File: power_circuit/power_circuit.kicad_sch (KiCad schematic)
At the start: 38 parts, among them J1 +, J10 Conn_01x02_Pin, J2 -, J7 Conn_01x02_Pin, M1 Fan, Q1 PMOS, Q2 PMOS, Q3 PMOS, Q4 PMOS, Q5 PMOS, Q6 PMOS, Q7 PMOS, Q8 PMOS, SW1 SW_SPDT, U1 LM76002RNPR, U2 STM32F042C6Tx, U3 TJA1051TK-3, U4 AMS1117-3.3

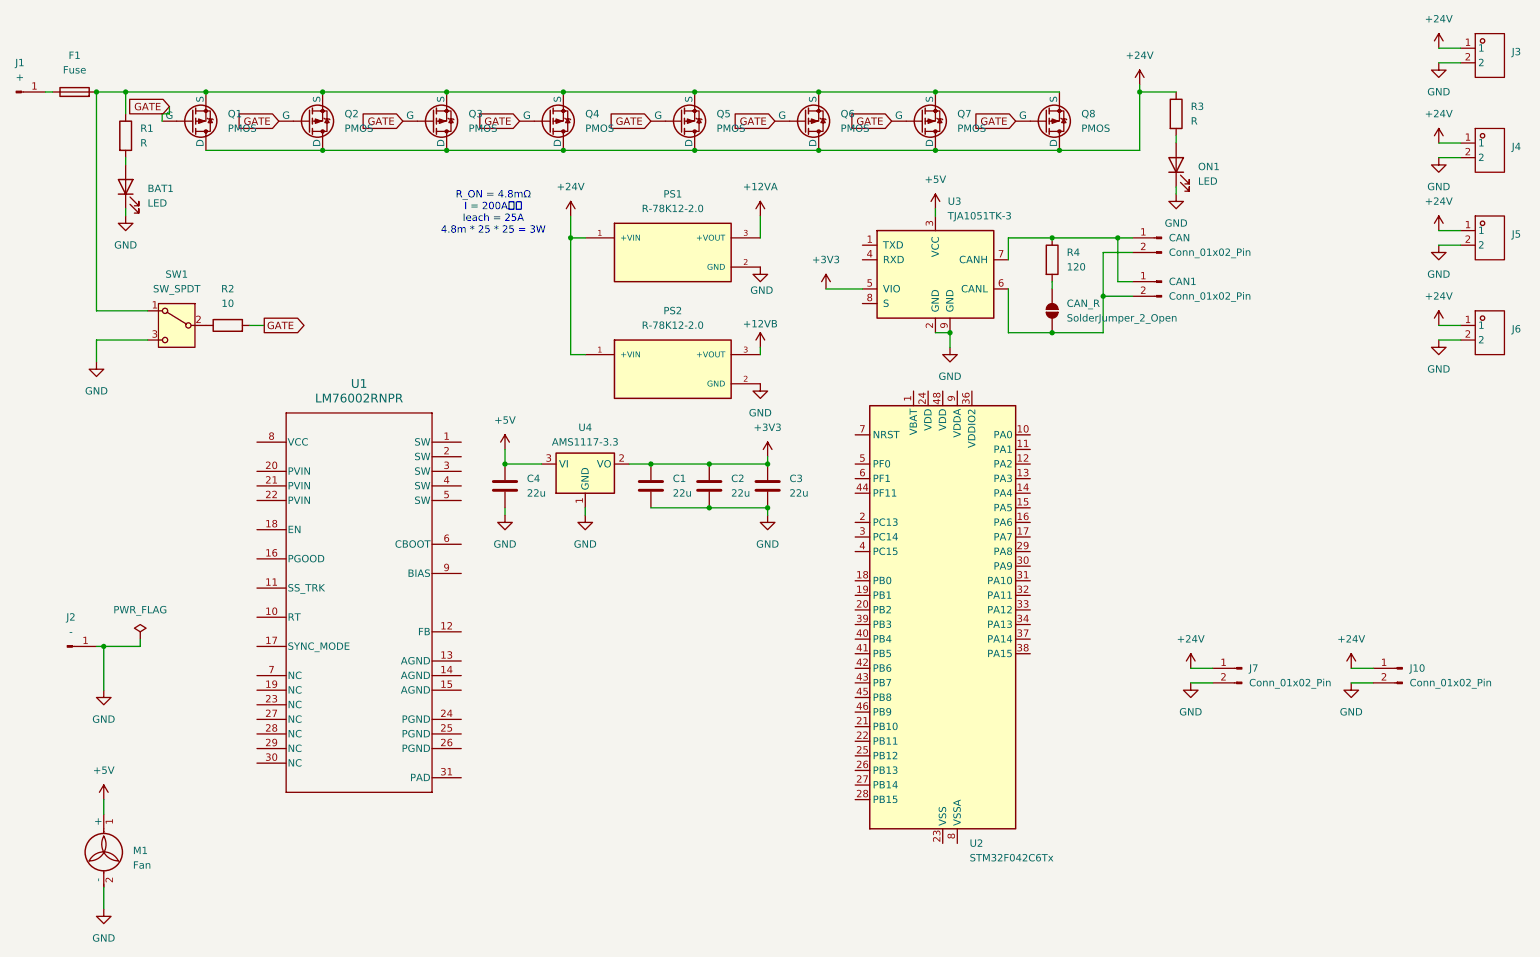
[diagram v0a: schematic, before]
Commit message: AQUA_VESC REV01作成
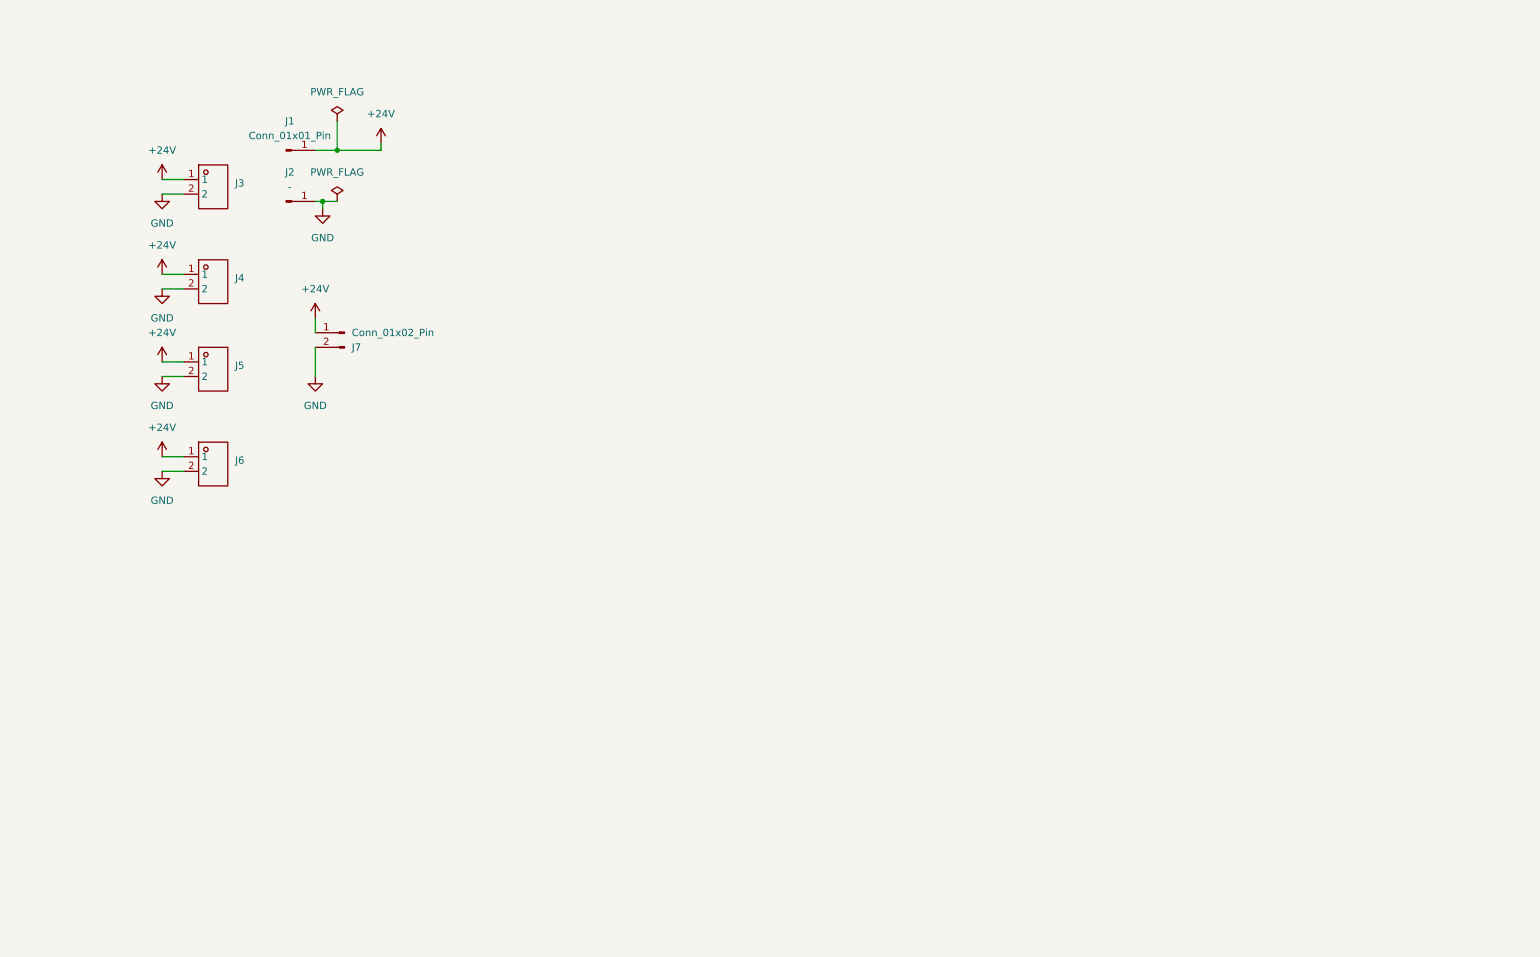
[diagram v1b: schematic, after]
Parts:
- removed BAT1, ON1: LED, symbol Device:LED
- removed C1, C2, C3, C4: 22u, symbol Device:C
- removed CAN, CAN1: Conn_01x02_Pin, Connector_JST:JST_XA_S02B-XASK-1_1x02_P2.50mm_Horizontal, symbol Connector:Conn_01x02_Pin
- removed CAN_R: SolderJumper_2_Open, symbol Jumper:SolderJumper_2_Open
- removed F1: Fuse, specific_footprint_library:anl_fuse, symbol Device:Fuse
- removed J10: Conn_01x02_Pin, Connector_JST:JST_VH_B2PS-VH_1x02_P3.96mm_Horizontal, symbol Connector:Conn_01x02_Pin
- removed M1: Fan, symbol Motor:Fan
- removed PS1, PS2: R-78K12-2.0, specific_footprint_library:CONV_R-78K12-2.0, symbol specific_library:R-78K12-2.0
- removed Q1, Q2, Q3, Q4, Q5, Q6, Q7, Q8: PMOS, symbol Simulation_SPICE:PMOS
- removed R1, R3: R, symbol Device:R
- removed R2: 10, symbol Device:R
- removed R4: 120, symbol Device:R
- removed SW1: SW_SPDT, symbol Switch:SW_SPDT
- removed U1: LM76002RNPR, specific_footprint_library:RNP0030B, symbol specific_library:LM76002RNPR
- removed U2: STM32F042C6Tx, Package_QFP:LQFP-48_7x7mm_P0.5mm, symbol MCU_ST_STM32F0:STM32F042C6Tx
- removed U3: TJA1051TK-3, Package_DFN_QFN:DFN-8-1EP_3x3mm_P0.65mm_EP1.55x2.4mm, symbol Interface_CAN_LIN:TJA1051TK-3
- removed U4: AMS1117-3.3, Package_TO_SOT_SMD:SOT-223-3_TabPin2, symbol Regulator_Linear:AMS1117-3.3
- J1: value + -> Conn_01x01_Pin; footprint MountingHole:MountingHole_5mm_Pad -> MountingHole:MountingHole_4.5mm_Pad_Via
- J2: footprint MountingHole:MountingHole_5mm_Pad -> MountingHole:MountingHole_4.5mm_Pad_Via
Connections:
- net +24V: now also J1.1 (Pin_1)
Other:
- note removed: "R_ON = 4.8mΩ I = 200Aの時 Ieach = 25A 4.8m * 25 * 25 = 3W"
- moved on the sheet: J2, J3, J4, J5, J6
